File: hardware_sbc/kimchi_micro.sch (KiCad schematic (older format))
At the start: 35 parts, among them J1 Conn_01x06, J2 Conn_01x06, J3 Conn_01x04_MountingPin, J4 Conn_02x05_Odd_Even, SW1 SW_Push, SW2 SW_Push, SW3 SW_Push, U1 IMX8MM, U2 24C32, Y1 Crystal_GND24

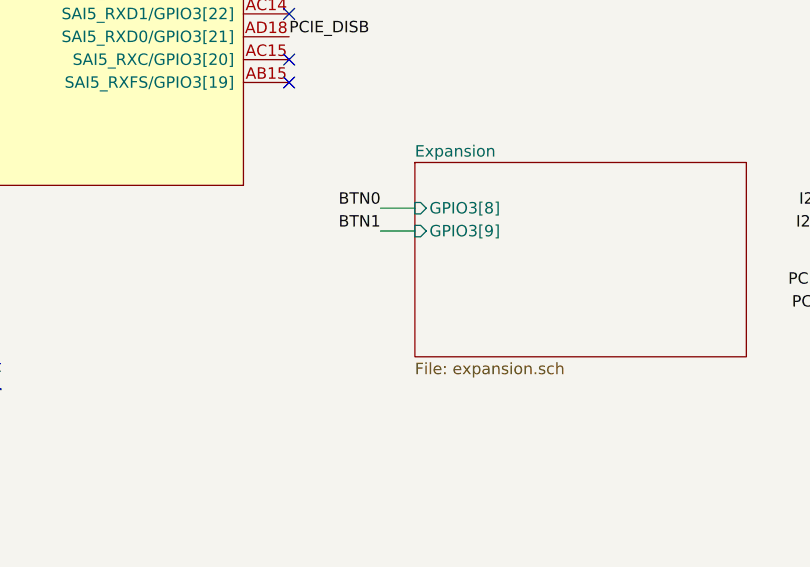
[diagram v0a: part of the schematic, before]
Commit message: Add vbus to expansion connector and bugfix for battery cutoff
This will allow lids to supply power to charge the battery.

The battery cutoff circuit needs V- connected to pack ground, so
this was also fixed.
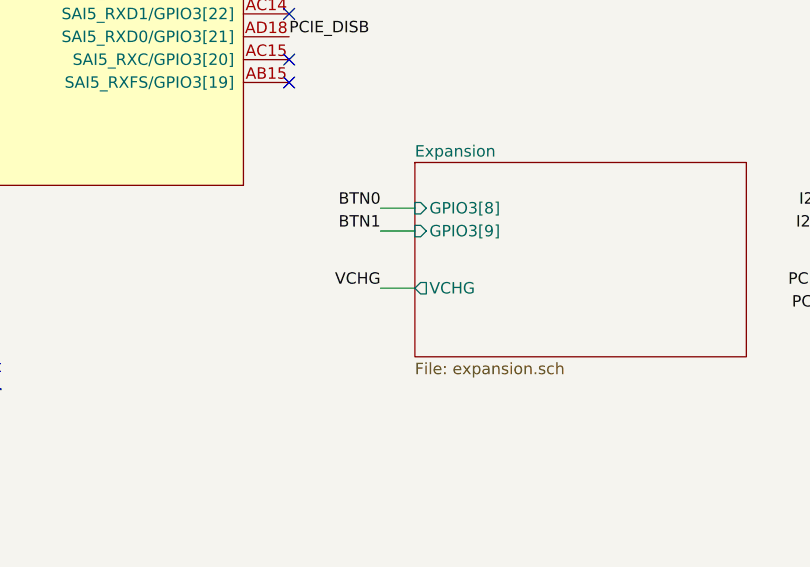
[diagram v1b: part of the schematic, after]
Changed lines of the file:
@@
 F2 "GPIO3[8]" I L 11000 5750 50
 F3 "GPIO3[9]" I L 11000 5850 50
+F4 "VCHG" O L 11000 6100 50
 $EndSheet
 Wire Wire Line
@@
 	0    -1   -1   0
 $EndComp
+Text Label 10850 6100 2    50   ~ 0
+VCHG
+Wire Wire Line
+	10850 6100 11000 6100
 $EndSCHEMATC
